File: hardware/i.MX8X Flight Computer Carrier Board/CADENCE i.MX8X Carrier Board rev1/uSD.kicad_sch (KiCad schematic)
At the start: 0 parts

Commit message: Sheet Organization
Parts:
- added C86: 100nF, symbol Device:C
- added C87: 10uF, symbol Device:C
- added J1: Micro_SD_Card_Det1, symbol Connector:Micro_SD_Card_Det1
- added R1, R104, R105, R106, R6, R7: 49.9k, symbol Device:R
- added R107, R108, R109, R110, R111: 22, symbol Device:R
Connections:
- new net: J1.2 (DAT3/CD), R110.1
- new net: J1.8 (DAT1), R107.1
- new net: J1.1 (DAT2), R111.1
- new net: J1.9 (DET), R106.1
- new net: J1.3 (CMD), R109.1
- new net: J1.7 (DAT0), R108.1
- new net +3.3V: C86.1, C87.1, J1.4 (VDD), R106.2
- new net GND: C86.2, C87.2, J1.10 (SHIELD), J1.6 (VSS)
- new net VCC_LDO_SD1: R1.2, R104.2, R105.2, R6.2, R7.2
- new net X_USDHC1_CLK: J1.5 (CLK), R7.1
- new net X_USDHC1_CMD/NAND_CE0_B: R109.2
- new net X_USDHC1_DATA0/NAND_CE1_B: R104.1, R108.2
- new net X_USDHC1_DATA1/NAND_RE_B: R105.1, R107.2
- new net X_USDHC1_DATA2/NAND_WE_B: R1.1, R111.2
- new net X_USDHC1_DATA3/NAND_ALE: R110.2, R6.1
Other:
- note added: "microSD"

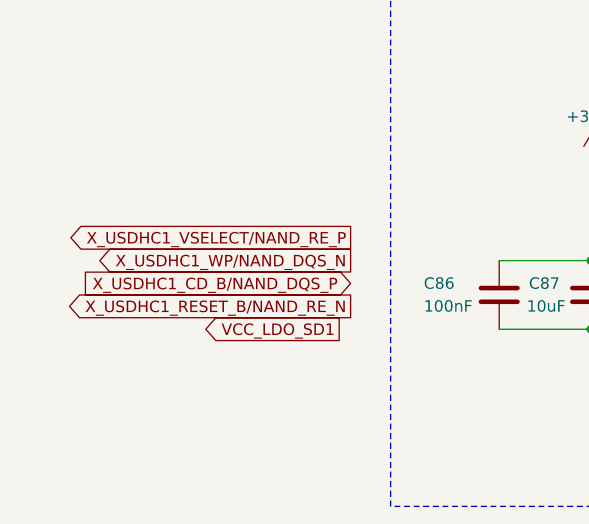
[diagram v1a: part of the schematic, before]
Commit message: added some LEDs, fixed few power nets
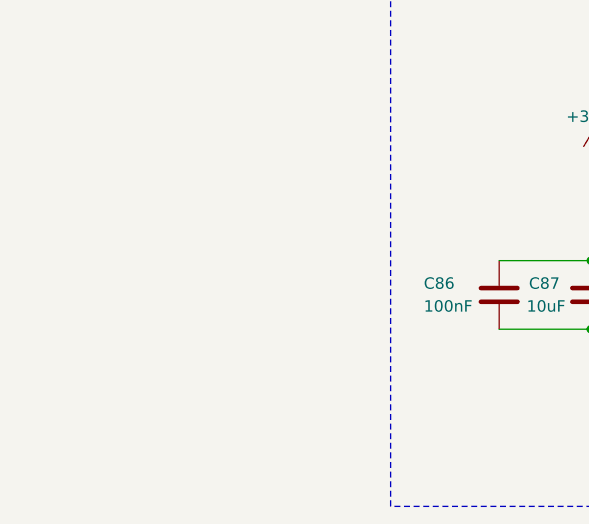
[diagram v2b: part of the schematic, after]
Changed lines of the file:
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@@
-		)
-	)
-	(global_label "X_USDHC1_WP/NAND_DQS_N"
-		(shape output)
-		(at 68.58 101.6 180)
-		(effects
-			(font
-				(size 1.27 1.27)
-			)
-			(justify right)
-		)
-		(property "Intersheetrefs" "${INTERSHEET_REFS}"
-			(at 68.58 101.6 0)
-			(effects
-				(font
-					(size 1.27 1.27)
-				)
-				(hide yes)
-			)
 		)
 	)
@@
 		)
 	)
-	(global_label "VCC_LDO_SD1"
-		(shape output)
-		(at 67.31 109.22 180)
-		(effects
-			(font
-				(size 1.27 1.27)
-			)
-			(justify right)
-		)
-		(property "Intersheetrefs" "${INTERSHEET_REFS}"
-			(at 67.31 109.22 0)
-			(effects
-				(font
-					(size 1.27 1.27)
-				)
-				(hide yes)
-			)
-		)
-	)
-	(global_label "X_USDHC1_VSELECT/NAND_RE_P"
-		(shape output)
-		(at 68.58 99.06 180)
-		(effects
-			(font
-				(size 1.27 1.27)
-			)
-			(justify right)
-		)
-		(property "Intersheetrefs" "${INTERSHEET_REFS}"
-			(at 68.58 99.06 0)
-			(effects
-				(font
-					(size 1.27 1.27)
-				)
-				(hide yes)
-			)
-		)
-	)
 	(global_label "X_USDHC1_DATA3/NAND_ALE"
 		(shape bidirectional)
@@
 			(effects
 				(font
-					(size 1.27 1.27)
-				)
-				(hide yes)
-			)
-		)
-	)
-	(global_label "X_USDHC1_RESET_B/NAND_RE_N"
-		(shape output)
-		(at 68.58 106.68 180)
-		(effects
-			(font
-				(size 1.27 1.27)
-			)
-			(justify right)
-		)
-		(property "Intersheetrefs" "${INTERSHEET_REFS}"
-			(at 68.58 106.68 0)
-			(effects
-				(font
-					(size 1.27 1.27)
-				)
-				(hide yes)
-			)
-		)
-	)
-	(global_label "X_USDHC1_CD_B/NAND_DQS_P"
-		(shape input)
-		(at 68.58 104.14 180)
-		(effects
-			(font
-				(size 1.27 1.27)
-			)
-			(justify right)
-		)
-		(property "Intersheetrefs" "${INTERSHEET_REFS}"
-			(at 68.58 104.14 0)
-			(effects
-				(font

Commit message: schematic reorg
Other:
- moved on the sheet: C86, C87, J1, R1, R104, R105, R106, R107, R108, R109, R110, R111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

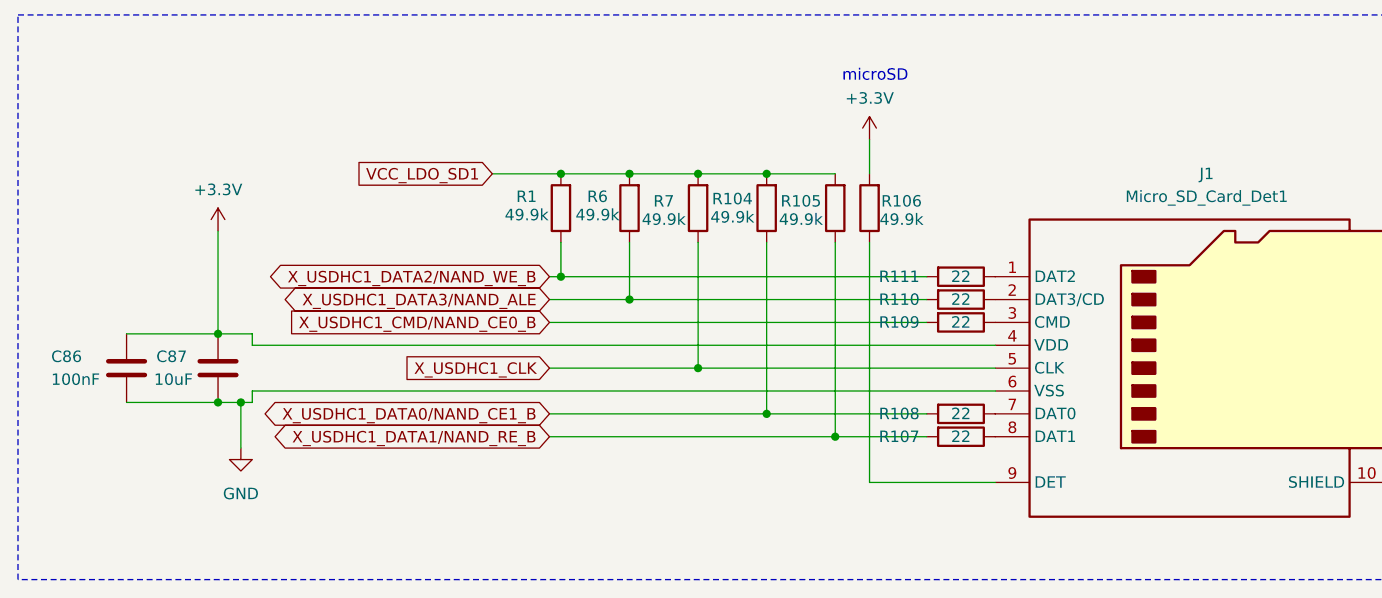
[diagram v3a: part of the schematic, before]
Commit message: added termination resistors for ebyte spi bus & fixed some erc issues
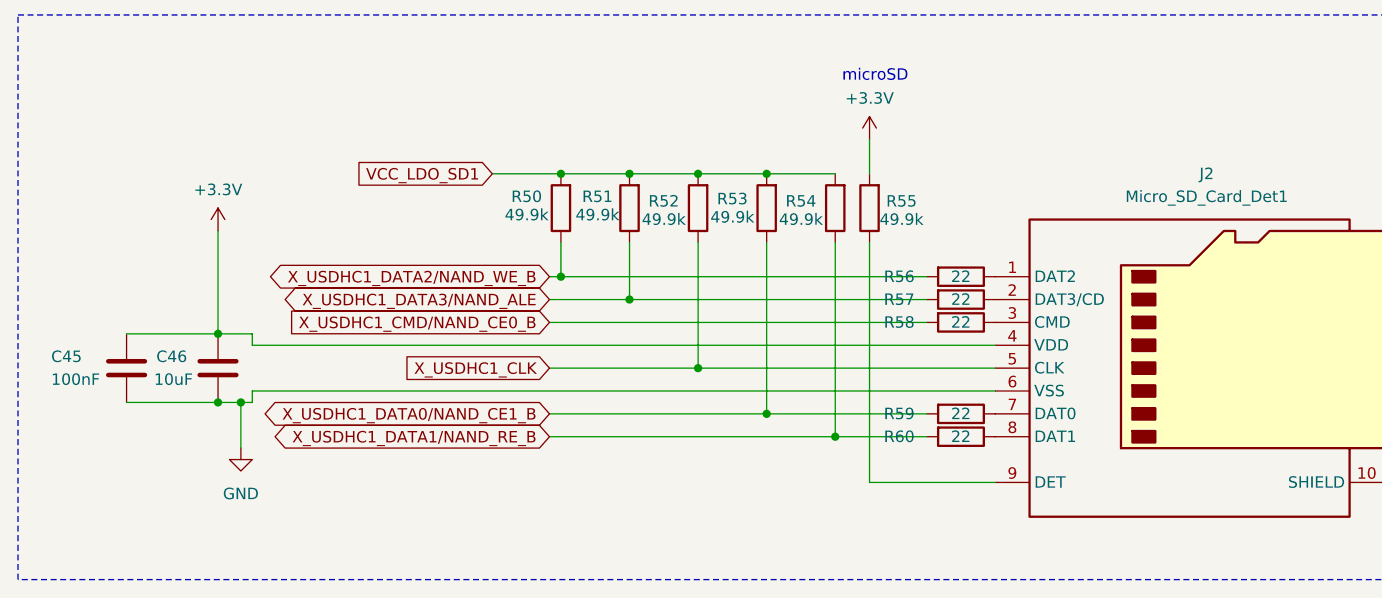
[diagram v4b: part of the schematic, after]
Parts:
- renumbered C86 to C45, C87 to C46, J1 to J2, R1 to R50, R6 to R51, R7 to R52, R104 to R53, R105 to R54, R106 to R55, R111 to R56, R110 to R57, R109 to R58, R108 to R59, R107 to R60
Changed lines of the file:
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@@
 		(on_board yes)
 		(dnp no)
-		(property "Reference" "R110"
+		(property "Reference" "R57"
 			(at 122.682 60.96 90)
 			(effects
@@
 			(project "CADENCE i.MX8X Carrier Board rev1"
 				(path "/de284495-d382-47cb-b528-76e440980d40/fe211871-5da0-4bfc-9ad4-60fa16dbacc5"
-					(reference "R110")
+					(reference "R57")
 					(unit 1)
 				)
@@
 		(on_board yes)
 		(dnp no)
-		(property "Reference" "R7"
+		(property "Reference" "R52"
 			(at 96.52 50.038 0)
 			(effects
@@
 			(project "CADENCE i.MX8X Carrier Board rev1"
 				(path "/de284495-d382-47cb-b528-76e440980d40/fe211871-5da0-4bfc-9ad4-60fa16dbacc5"
-					(reference "R7")
+					(reference "R52")
 					(unit 1)
 				)
@@
 		(on_board yes)
 		(dnp no)
-		(property "Reference" "R107"
+		(property "Reference" "R60"
 			(at 122.682 76.2 90)
 			(effects
@@
 			(project "CADENCE i.MX8X Carrier Board rev1"
 				(path "/de284495-d382-47cb-b528-76e440980d40/fe211871-5da0-4bfc-9ad4-60fa16dbacc5"
-					(reference "R107")
+					(reference "R60")
 					(unit 1)
 				)
@@
 		(on_board yes)
 		(dnp no)
-		(property "Reference" "R1"
+		(property "Reference" "R50"
 			(at 81.28 49.53 0)
 			(effects
@@
 			(project "CADENCE i.MX8X Carrier Board rev1"
 				(path "/de284495-d382-47cb-b528-76e440980d40/fe211871-5da0-4bfc-9ad4-60fa16dbacc5"
-					(reference "R1")
+					(reference "R50")
 					(unit 1)
 				)
@@
 		(on_board yes)
 		(dnp no)
-		(property "Reference" "R111"
+		(property "Reference" "R56"
 			(at 122.682 58.42 90)
 			(effects
@@
 			(project "CADENCE i.MX8X Carrier Board rev1"
 				(path "/de284495-d382-47cb-b528-76e440980d40/fe211871-5da0-4bfc-9ad4-60fa16dbacc5"
-					(reference "R111")
+					(reference "R56")
 					(unit 1)
 				)
@@
 		(on_board yes)
 		(dnp no)
-		(property "Reference" "R106"
+		(property "Reference" "R55"
 			(at 122.936 50.038 0)
 			(effects
@@
 			(project "CADENCE i.MX8X Carrier Board rev1"
 				(path "/de284495-d382-47cb-b528-76e440980d40/fe211871-5da0-4bfc-9ad4-60fa16dbacc5"
-					(reference "R106")
+					(reference "R55")
 					(unit 1)
 				)
@@
 		(dnp no)
 		(fields_autoplaced yes)
-		(property "Reference" "J1"
+		(property "Reference" "J2"
 			(at 156.845 46.99 0)
 			(effects
@@
 			(project "CADENCE i.MX8X Carrier Board rev1"
 				(path "/de284495-d382-47cb-b528-76e440980d40/fe211871-5da0-4bfc-9ad4-60fa16dbacc5"
-					(reference "J1")
+					(reference "J2")
 					(unit 1)
 				)
@@
 		(dnp no)
 		(fields_autoplaced yes)
-		(property "Reference" "#PWR0139"
+		(property "Reference" "#PWR054"
 			(at 180.34 88.9 0)
 			(effects
@@
 			(project "CADENCE i.MX8X Carrier Board rev1"
 				(path "/de284495-d382-47cb-b528-76e440980d40/fe211871-5da0-4bfc-9ad4-60fa16dbacc5"
-					(reference "#PWR0139")
+					(reference "#PWR054")
 					(unit 1)
 				)
@@
 		(on_board yes)
 		(dnp no)
-		(property "Reference" "R104"
+		(property "Reference" "R53"
 			(at 104.14 49.784 0)
 			(effects
@@
 			(project "CADENCE i.MX8X Carrier Board rev1"
 				(path "/de284495-d382-47cb-b528-76e440980d40/fe211871-5da0-4bfc-9ad4-60fa16dbacc5"
-					(reference "R104")
+					(reference "R53")
 					(unit 1)
 				)
@@
 		(on_board yes)
 		(dnp no)
-		(property "Reference" "C86"
+		(property "Reference" "C45"
 			(at 28.448 67.31 0)
 			(effects
@@
 			(project "CADENCE i.MX8X Carrier Board rev1"
 				(path "/de284495-d382-47cb-b528-76e440980d40/fe211871-5da0-4bfc-9ad4-60fa16dbacc5"
-					(reference "C86")
+					(reference "C45")
 					(unit 1)
 				)
@@
 		(dnp no)
 		(fields_autoplaced yes)
-		(property "Reference" "#PWR012"
+		(property "Reference" "#PWR052"
 			(at 49.53 83.82 0)
 			(effects
@@
 			(project "CADENCE i.MX8X Carrier Board rev1"
 				(path "/de284495-d382-47cb-b528-76e440980d40/fe211871-5da0-4bfc-9ad4-60fa16dbacc5"
-					(reference "#PWR012")
+					(reference "#PWR052")
 					(unit 1)
 				)
@@
 		(on_board yes)
 		(dnp no)
-		(property "Reference" "R108"
+		(property "Reference" "R59"
 			(at 122.682 73.66 90)
 			(effects
@@
 			(project "CADENCE i.MX8X Carrier Board rev1"
 				(path "/de284495-d382-47cb-b528-76e440980d40/fe211871-5da0-4bfc-9ad4-60fa16dbacc5"
-					(reference "R108")
+					(reference "R59")
 					(unit 1)
 				)
@@
 		(on_board yes)
 		(dnp no)
-		(property "Reference" "R105"
+		(property "Reference" "R54"
 			(at 111.76 50.038 0)
 			(effects
@@
 			(project "CADENCE i.MX8X Carrier Board rev1"
 				(path "/de284495-d382-47cb-b528-76e440980d40/fe211871-5da0-4bfc-9ad4-60fa16dbacc5"
-					(reference "R105")
+					(reference "R54")
 					(unit 1)
 				)
@@
 		(on_board yes)
 		(dnp no)
-		(property "Reference" "R6"
+		(property "Reference" "R51"
 			(at 89.154 49.53 0)
 			(effects
@@
 			(project "CADENCE i.MX8X Carrier Board rev1"
 				(path "/de284495-d382-47cb-b528-76e440980d40/fe211871-5da0-4bfc-9ad4-60fa16dbacc5"
-					(reference "R6")
+					(reference "R51")
 					(unit 1)
 				)
@@
 		(on_board yes)
 		(dnp no)
-		(property "Reference" "C87"
+		(property "Reference" "C46"
 			(at 40.132 67.31 0)
 			(effects
@@
 			(project "CADENCE i.MX8X Carrier Board rev1"
 				(path "/de284495-d382-47cb-b528-76e440980d40/fe211871-5da0-4bfc-9ad4-60fa16dbacc5"
-					(reference "C87")
+					(reference "C46")
 					(unit 1)
 				)
@@
 		(on_board yes)
 		(dnp no)
-		(property "Reference" "#PWR014"
+		(property "Reference" "#PWR053"
 			(at 119.38 46.99 0)
 			(effects
@@
 			(project "CADENCE i.MX8X Carrier Board rev1"
 				(path "/de284495-d382-47cb-b528-76e440980d40/fe211871-5da0-4bfc-9ad4-60fa16dbacc5"
-					(reference "#PWR014")
+					(reference "#PWR053")
 					(unit 1)
 				)
@@
 		(on_board yes)
 		(dnp no)
-		(property "Reference" "R109"
+		(property "Reference" "R58"
 			(at 122.682 63.5 90)
 			(effects
@@
 			(project "CADENCE i.MX8X Carrier Board rev1"
 				(path "/de284495-d382-47cb-b528-76e440980d40/fe211871-5da0-4bfc-9ad4-60fa16dbacc5"
-					(reference "R109")
+					(reference "R58")
 					(unit 1)
 				)
@@
 		(on_board yes)
 		(dnp no)
-		(property "Reference" "#PWR0138"
+		(property "Reference" "#PWR051"
 			(at 46.99 57.15 0)
 			(effects
@@
 			(project "CADENCE i.MX8X Carrier Board rev1"
 				(path "/de284495-d382-47cb-b528-76e440980d40/fe211871-5da0-4bfc-9ad4-60fa16dbacc5"
-					(reference "#PWR0138")
-					(unit 1)
-				)
+					(reference "#PWR051")
+					(unit 1)
+				)

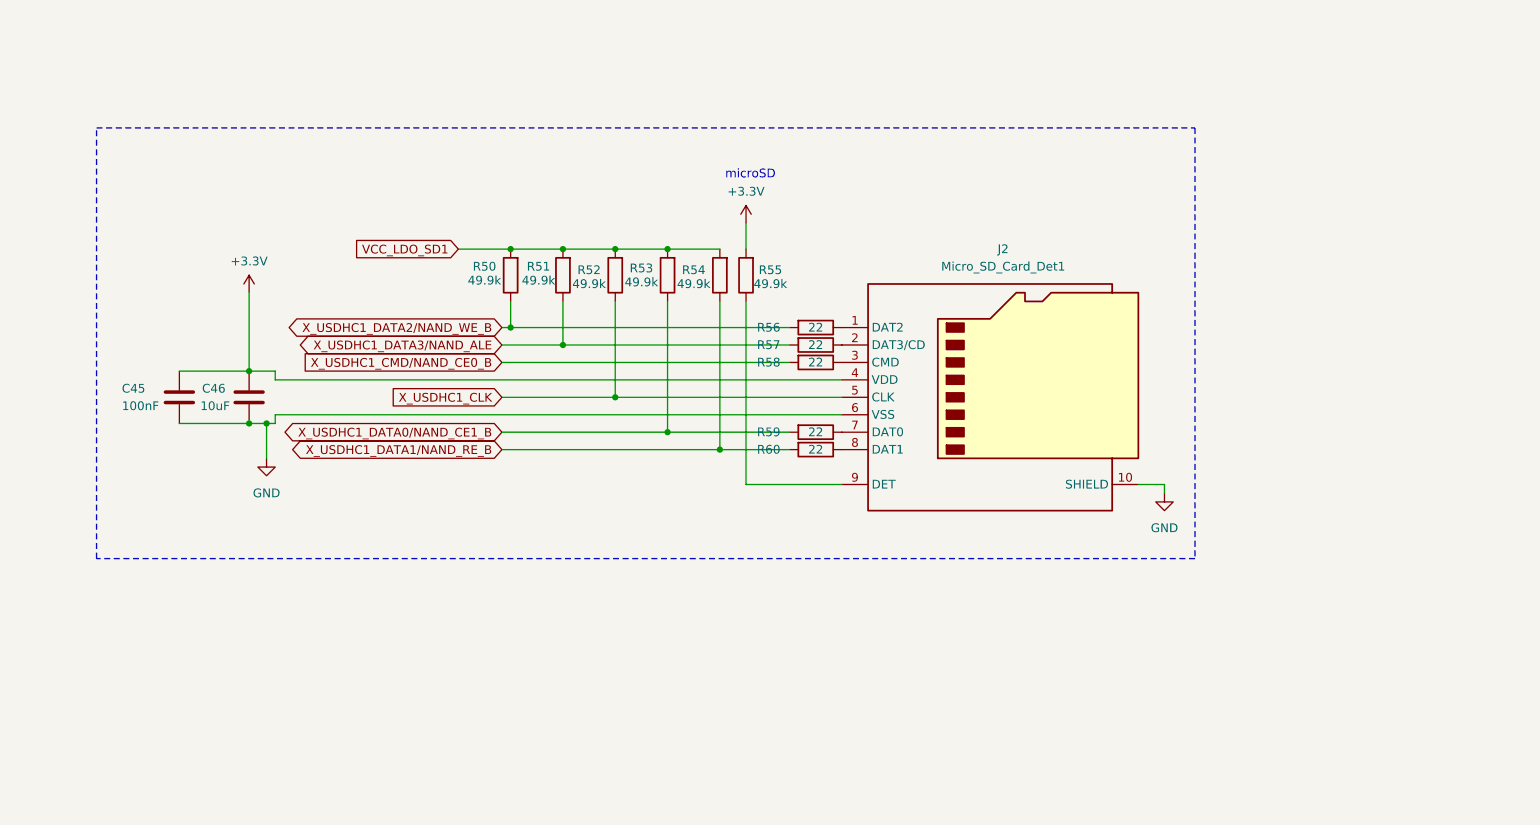
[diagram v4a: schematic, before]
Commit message: Added pin definitions page
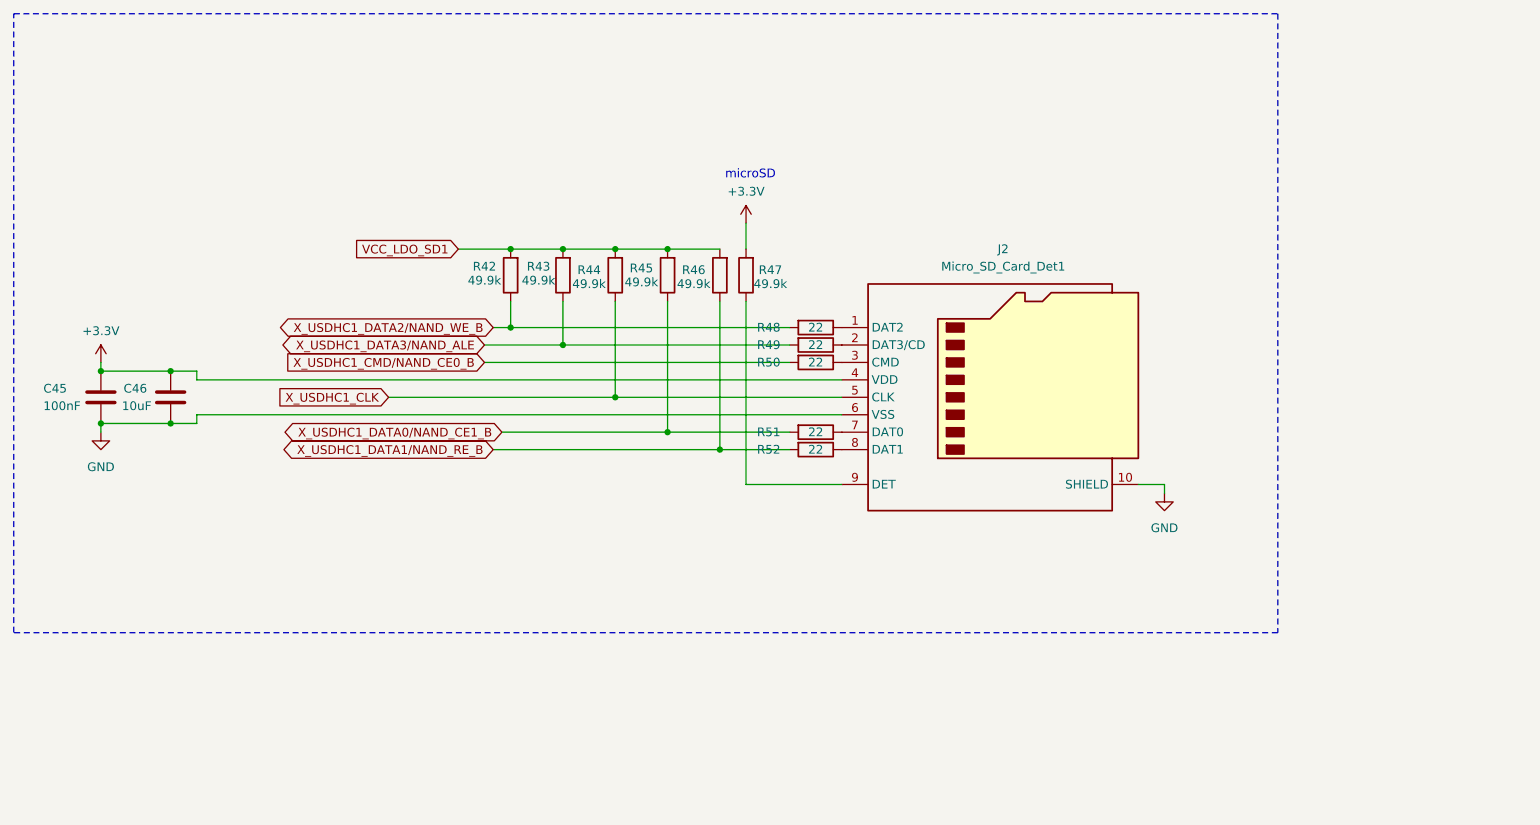
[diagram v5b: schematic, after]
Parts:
- renumbered R50 to R42, R51 to R43, R52 to R44, R53 to R45, R54 to R46, R55 to R47, R56 to R48, R57 to R49, R58 to R50, R59 to R51, R60 to R52
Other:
- moved on the sheet: C45, C46

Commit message: updated footprints for system control and usd schematic
Might need to make a footprint for the power switch, since i couldn't find anything online
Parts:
- J2: footprint (none) -> Footprints:TF-SMD_XKTF-015-N
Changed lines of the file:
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@@
 			)
 		)
-		(property "Footprint" ""
+		(property "Footprint" "Footprints:TF-SMD_XKTF-015-N"
 			(at 208.28 50.8 0)
 			(effects

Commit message: added footprints to imx8x, just need to finish usb, capacitors, and inductors
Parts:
- C45, C46: footprint (none) -> Capacitor_SMD:C_0603_1608Metric
- R42, R43, R44, R45, R46, R47, R48, R49, R50, R51, R52: footprint (none) -> Resistor_SMD:R_0402_1005Metric
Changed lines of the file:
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@@
 			)
 		)
-		(property "Footprint" ""
+		(property "Footprint" "Resistor_SMD:R_0402_1005Metric"
 			(at 129.54 59.182 90)
 			(effects
@@
 			)
 		)
-		(property "Footprint" ""
+		(property "Footprint" "Resistor_SMD:R_0402_1005Metric"
 			(at 102.108 50.8 90)
 			(effects
@@
 			)
 		)
-		(property "Footprint" ""
+		(property "Footprint" "Resistor_SMD:R_0402_1005Metric"
 			(at 129.54 74.422 90)
 			(effects
@@
 			)
 		)
-		(property "Footprint" ""
+		(property "Footprint" "Resistor_SMD:R_0402_1005Metric"
 			(at 86.868 50.8 90)
 			(effects
@@
 			)
 		)
-		(property "Footprint" ""
+		(property "Footprint" "Resistor_SMD:R_0402_1005Metric"
 			(at 129.54 56.642 90)
 			(effects
@@
 			)
 		)
-		(property "Footprint" ""
+		(property "Footprint" "Resistor_SMD:R_0402_1005Metric"
 			(at 121.158 50.8 90)
 			(effects
@@
 			)
 		)
-		(property "Footprint" ""
+		(property "Footprint" "Resistor_SMD:R_0402_1005Metric"
 			(at 109.728 50.8 90)
 			(effects
@@
 			)
 		)
-		(property "Footprint" ""
+		(property "Footprint" "Capacitor_SMD:C_0603_1608Metric"
 			(at 26.3652 72.39 0)
 			(effects
@@
 			)
 		)
-		(property "Footprint" ""
+		(property "Footprint" "Resistor_SMD:R_0402_1005Metric"
 			(at 129.54 71.882 90)
 			(effects
@@
 			)
 		)
-		(property "Footprint" ""
+		(property "Footprint" "Resistor_SMD:R_0402_1005Metric"
 			(at 117.348 50.8 90)
 			(effects
@@
 			)
 		)
-		(property "Footprint" ""
+		(property "Footprint" "Resistor_SMD:R_0402_1005Metric"
 			(at 94.488 50.8 90)
 			(effects
@@
 			)
 		)
-		(property "Footprint" ""
+		(property "Footprint" "Capacitor_SMD:C_0603_1608Metric"
 			(at 36.5252 72.39 0)
 			(effects
@@
 			)
 		)
-		(property "Footprint" ""
+		(property "Footprint" "Resistor_SMD:R_0402_1005Metric"
 			(at 129.54 61.722 90)
 			(effects
